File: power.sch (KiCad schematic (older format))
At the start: 7 parts

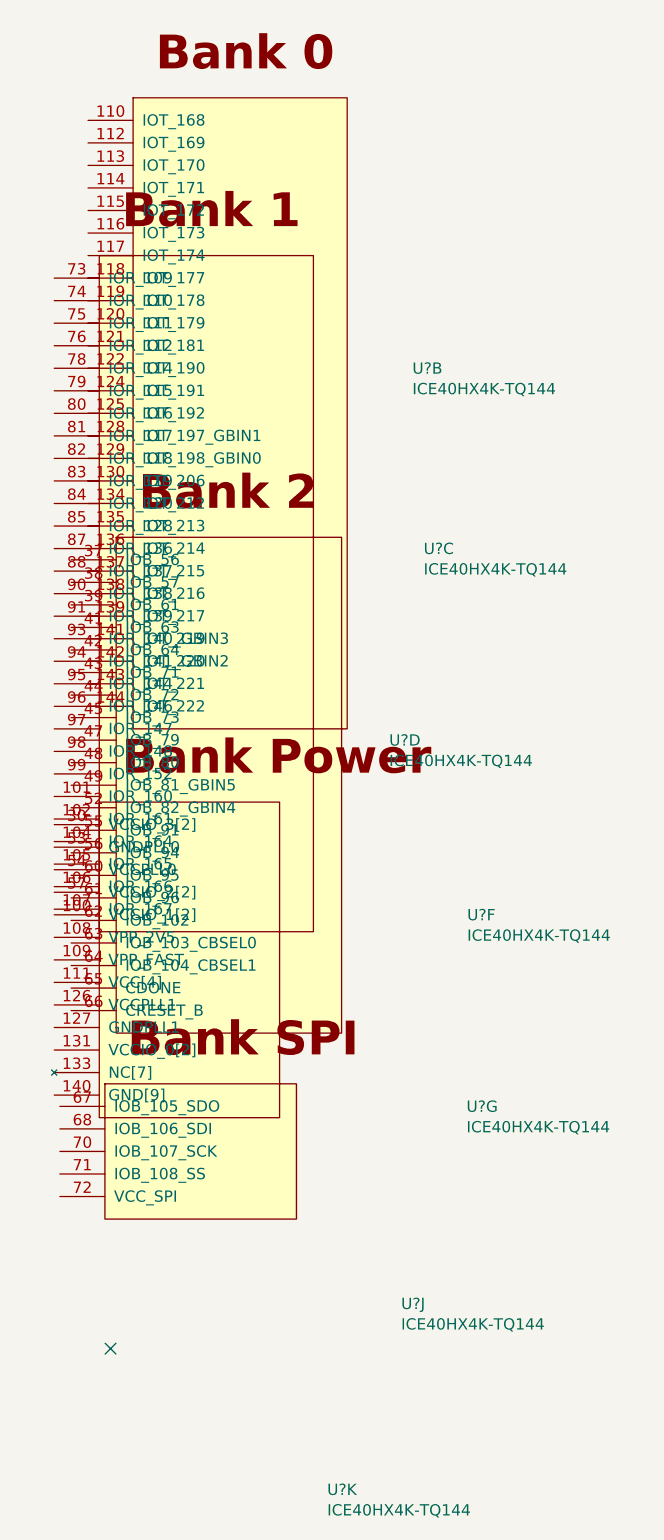
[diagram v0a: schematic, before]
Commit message: Made a overview on the toplevel schematic and added the SRAM subschematic.
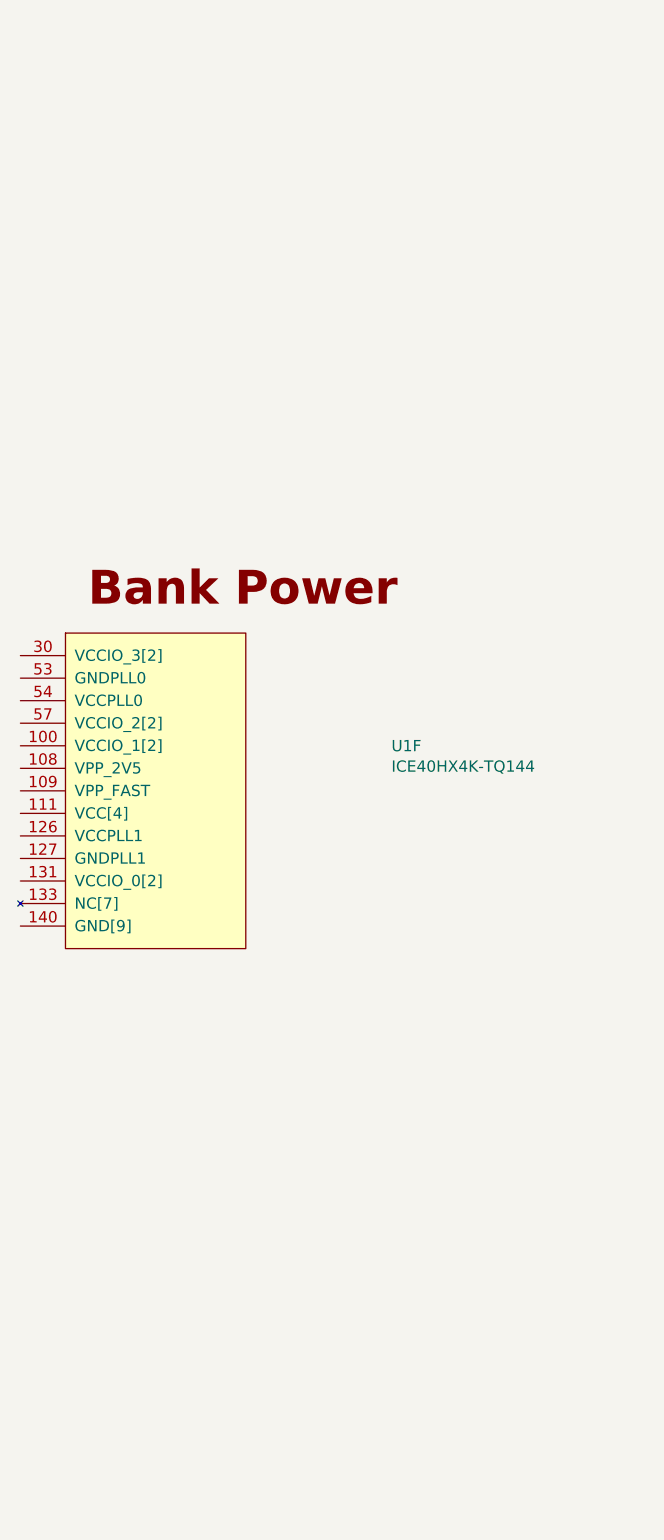
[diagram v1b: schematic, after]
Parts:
- removed U? (x7): ICE40HX4K-TQ144, symbol ice40hx4k:ICE40HX4K-TQ144
- added U1: ICE40HX4K-TQ144, symbol ice40hx4k:ICE40HX4K-TQ144
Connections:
- new net: U1.100 (VCCIO_1[2]), U1.89 (VCCIO_1)
- new net: U1.103 (GND), U1.13 (GND), U1.132 (GND), U1.14 (GND), U1.140 (GND[9]), U1.5 (GND), U1.59 (GND), U1.69 (GND), U1.86 (GND)
- new net: U1.111 (VCC[4]), U1.27 (VCC), U1.40 (VCC), U1.92 (VCC)
- new net: U1.123 (VCCIO_0), U1.131 (VCCIO_0[2])
- new net: U1.133 (NC[7]), U1.35 (NC), U1.36 (NC), U1.50 (NC), U1.51 (NC), U1.58 (NC), U1.77 (NC)
- new net: U1.30 (VCCIO_3[2]), U1.6 (VCCIO_3)
- new net: U1.46 (VCCIO_2), U1.57 (VCCIO_2[2])
- no-connect marks 1 -> 0
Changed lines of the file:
@@
 EESchema Schematic File Version 4
+LIBS:ice40_breakout-cache
 EELAYER 29 0
 EELAYER END
 $Descr A4 11693 8268
 encoding utf-8
-Sheet 2 5
+Sheet 2 6
 Title ""
 Date ""
@@
 $EndDescr
 $Comp
-L ice40hx4k:ICE40HX4K-TQ144 U?
-U 2 1 5CA8FCE6
-P 8850 1025
-F 0 "U?" H 10089 1224 50  0000 L CNN
-F 1 "ICE40HX4K-TQ144" H 10089 1133 50  0000 L CNN
-F 2 "" H 8850 1025 50  0001 C CNN
-F 3 "" H 8850 1025 50  0001 C CNN
-	2    8850 1025
+L ice40hx4k:ICE40HX4K-TQ144 U1
+U 6 1 5CAC0C63
+P 8550 2700
+F 0 "U1" H 9996 2899 50  0000 L CNN
+F 1 "ICE40HX4K-TQ144" H 9996 2808 50  0000 L CNN
+F 2 "" H 8550 2700 50  0001 C CNN
+F 3 "" H 8550 2700 50  0001 C CNN
+	6    8550 2700
 	1    0    0    -1
 $EndComp
-$Comp
-L ice40hx4k:ICE40HX4K-TQ144 U?
-U 3 1 5CA93257
-P 8700 1825
-F 0 "U?" H 10139 2024 50  0000 L CNN
-F 1 "ICE40HX4K-TQ144" H 10139 1933 50  0000 L CNN
-F 2 "" H 8700 1825 50  0001 C CNN
-F 3 "" H 8700 1825 50  0001 C CNN
-	3    8700 1825
-	1    0    0    -1
-$EndComp
-$Comp
-L ice40hx4k:ICE40HX4K-TQ144 U?
-U 4 1 5CA9530D
-P 8775 2675
-F 0 "U?" H 9986 2874 50  0000 L CNN
-F 1 "ICE40HX4K-TQ144" H 9986 2783 50  0000 L CNN
-F 2 "" H 8775 2675 50  0001 C CNN
-F 3 "" H 8775 2675 50  0001 C CNN
-	4    8775 2675
-	1    0    0    -1
-$EndComp
-$Comp
-L ice40hx4k:ICE40HX4K-TQ144 U?
-U 6 1 5CA97B84
-P 8700 3450
-F 0 "U?" H 10332 3649 50  0000 L CNN
-F 1 "ICE40HX4K-TQ144" H 10332 3558 50  0000 L CNN
-F 2 "" H 8700 3450 50  0001 C CNN
-F 3 "" H 8700 3450 50  0001 C CNN
-	6    8700 3450
-	1    0    0    -1
-$EndComp
-$Comp
-L ice40hx4k:ICE40HX4K-TQ144 U?
-U 7 1 5CA99D54
-P 8725 4300
-F 0 "U?" H 10329 4499 50  0000 L CNN
-F 1 "ICE40HX4K-TQ144" H 10329 4408 50  0000 L CNN
-F 2 "" H 8725 4300 50  0001 C CNN
-F 3 "" H 8725 4300 50  0001 C CNN
-	7    8725 4300
-	1    0    0    -1
-$EndComp
-$Comp
-L ice40hx4k:ICE40HX4K-TQ144 U?
-U 11 1 5CAA18F5
-P 8500 6000
-F 0 "U?" H 9711 6199 50  0000 L CNN
-F 1 "ICE40HX4K-TQ144" H 9711 6108 50  0000 L CNN
-F 2 "" H 8500 6000 50  0001 C CNN
-F 3 "" H 8500 6000 50  0001 C CNN
-	11   8500 6000
-	1    0    0    -1
-$EndComp
-$Comp
-L ice40hx4k:ICE40HX4K-TQ144 U?
-U 10 1 5CA9C21C
-P 8950 5175
-F 0 "U?" H 10039 5374 50  0000 L CNN
-F 1 "ICE40HX4K-TQ144" H 10039 5283 50  0000 L CNN
-F 2 "" H 8950 5175 50  0001 C CNN
-F 3 "" H 8950 5175 50  0001 C CNN
-	10   8950 5175
-	1    0    0    -1
-$EndComp
-NoConn ~ 8750 5175
 $EndSCHEMATC

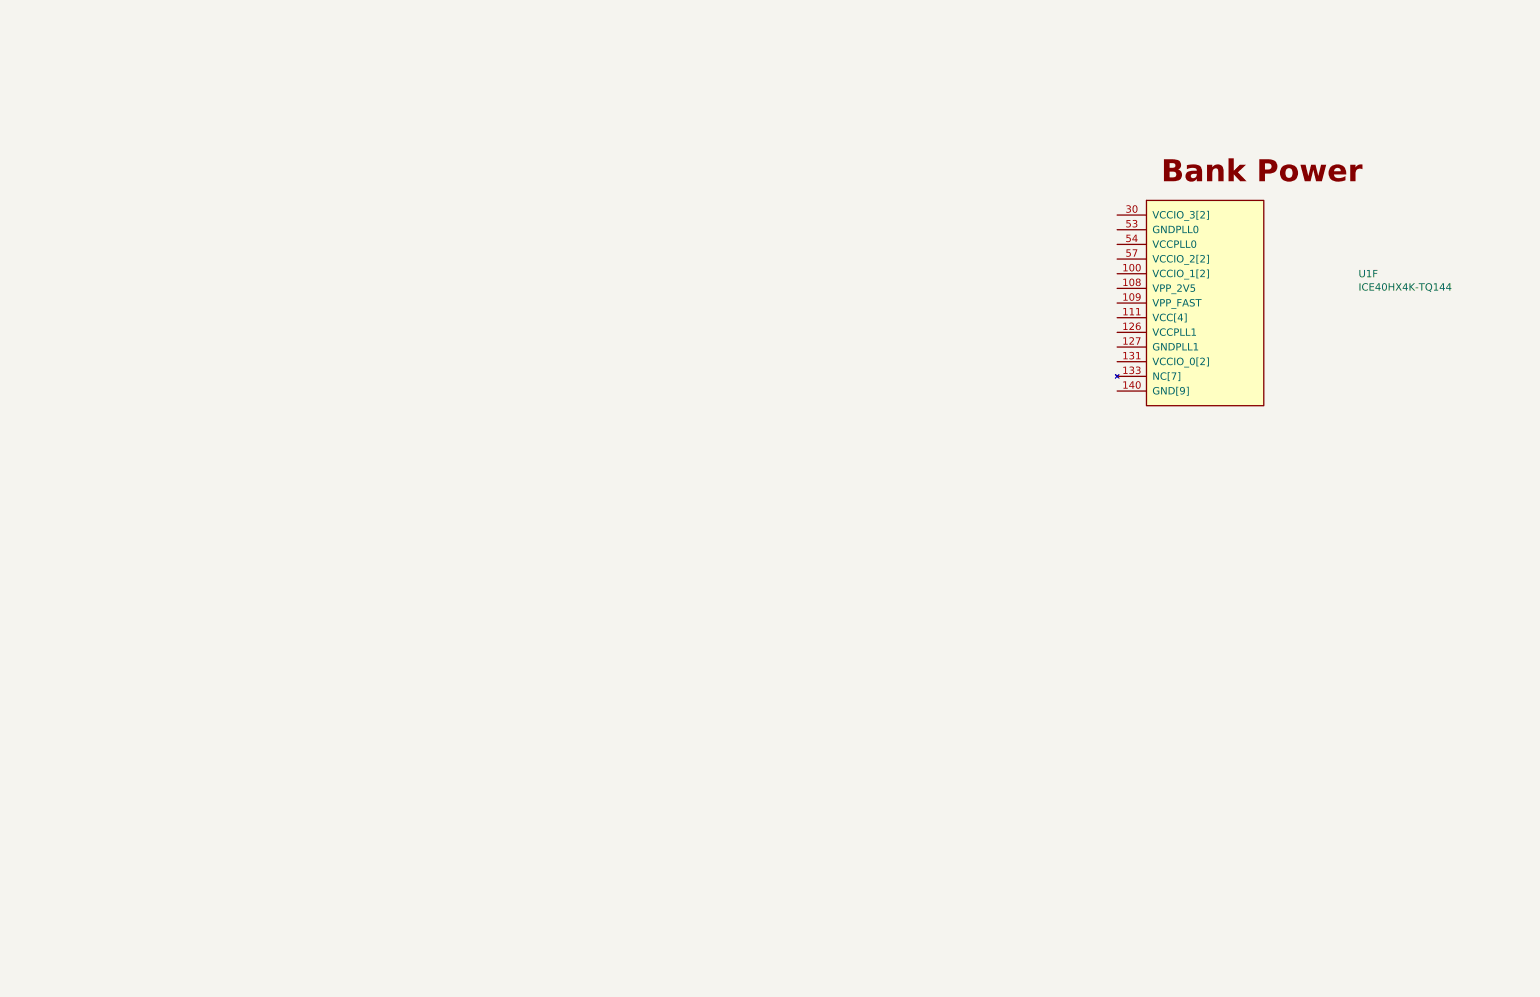
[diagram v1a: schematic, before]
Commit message: sram, ui, power, flash and header
SRAM: mostly done. Changed the choosen IC to a faster one in a differenc housing.

POWER: added some step down converter for 3.3 V and 1.2 V. The 1.2 V is oversized and could be changed to a smaller one

Programmer: added flash.

HEADER: Added Arduino Uno like headers with 5 V signal level. Analog is not connected now, will get an I2C ADC in future. Also added 3 digilent pmod styled connector with 3.3 V signal level.

UI: added 5 buttons and 8 LEDs. There is some space left over, maybe double the LED count in future.
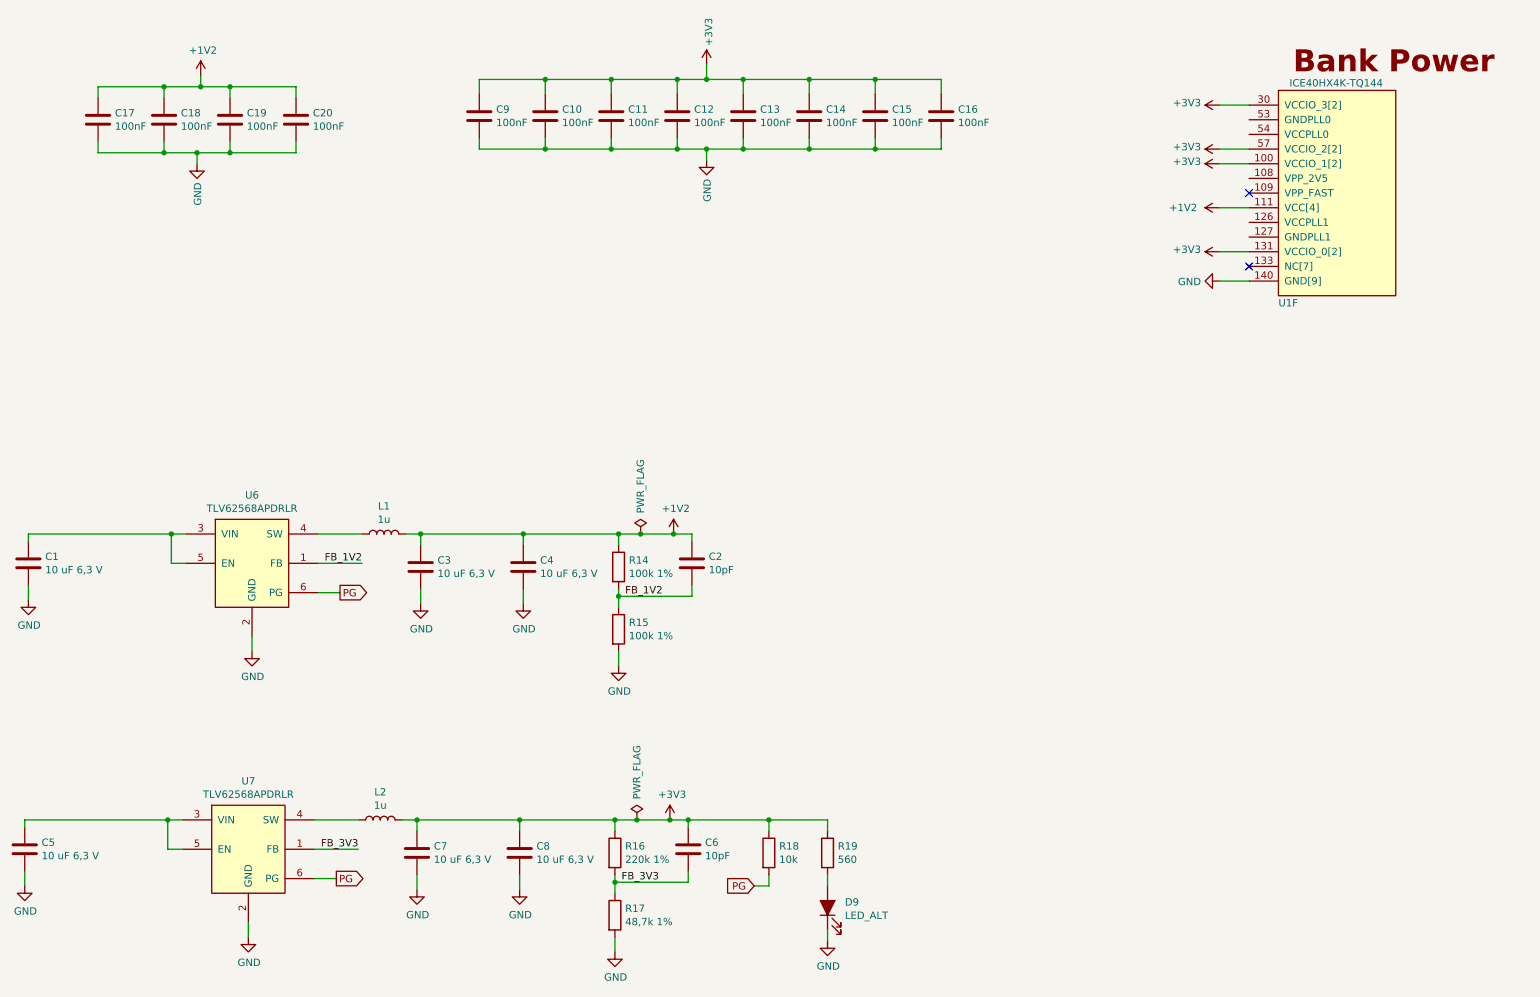
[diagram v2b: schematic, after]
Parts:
- added C1, C3, C4, C5, C7, C8: 10 uF 6,3 V, Capacitor_SMD:C_0603_1608Metric, symbol Device:C
- added C10, C11, C12, C13, C14, C15, C16, C17, C18, C19, C20, C9: 100nF, Capacitor_SMD:C_0603_1608Metric, symbol Device:C
- added C2, C6: 10pF, Capacitor_SMD:C_0603_1608Metric, symbol Device:C
- added D9: LED_ALT, LED_SMD:LED_0603_1608Metric, symbol Device:LED_ALT
- added L1, L2: 1u, footprints:L_1008_2520Metric_2.5x2mm_footprint, symbol Device:L
- added R14, R15: 100k 1%, Resistor_SMD:R_0603_1608Metric, symbol Device:R
- added R16: 220k 1%, Resistor_SMD:R_0603_1608Metric, symbol Device:R
- added R17: 48,7k 1%, Resistor_SMD:R_0603_1608Metric, symbol Device:R
- added R18: 10k, Resistor_SMD:R_0603_1608Metric, symbol Device:R
- added R19: 560, Resistor_SMD:R_0603_1608Metric, symbol Device:R
- added U6, U7: TLV62568APDRLR, Package_TO_SOT_SMD:SOT-563, symbol TLV62568APDRLR:TLV62568APDRLR
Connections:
- net +3V3: now reaches U1.100 (VCCIO_1[2]), U1.89 (VCCIO_1)
- net +3V3: now also U1.123 (VCCIO_0), U1.131 (VCCIO_0[2]), U1.30 (VCCIO_3[2]), U1.46 (VCCIO_2), U1.57 (VCCIO_2[2]), U1.6 (VCCIO_3), C10.1, C11.1, C12.1, C13.1, C14.1, C15.1, C16.1, C6.1, C7.1, C8.1, C9.1, L2.2, R16.1, R18.1, R19.1
- net GND: now reaches U1.103 (GND), U1.13 (GND), U1.132 (GND), U1.14 (GND), U1.140 (GND[9]), U1.5 (GND), U1.59 (GND), U1.69 (GND), U1.86 (GND)
- net GND: now also C1.2, C10.2, C11.2, C12.2, C13.2, C14.2, C15.2, C16.2, C17.2, C18.2, C19.2, C20.2, C3.2, C4.2, C5.2, C7.2, C8.2, C9.2, D9.1 (K), R15.2, R17.2, U6.2 (GND), U7.2 (GND)
- net +1V2: now reaches U1.111 (VCC[4]), U1.27 (VCC), U1.40 (VCC), U1.92 (VCC)
- net +1V2: now also C17.1, C18.1, C19.1, C2.1, C20.1, C3.1, C4.1, L1.2, R14.1
- new net: C1.1, U6.3 (VIN), U6.5 (EN)
- new net: L1.1, U6.4 (SW)
- new net: C5.1, U7.3 (VIN), U7.5 (EN)
- new net: L2.1, U7.4 (SW)
- new net: D9.2 (A), R19.2
- new net FB_1V2: C2.2, R14.2, R15.1, U6.1 (FB)
- new net FB_3V3: C6.2, R16.2, R17.1, U7.1 (FB)
- new net PG: R18.2, U6.6 (PG), U7.6 (PG)
- no-connect marks 0 -> 2
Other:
- moved on the sheet: U1F
